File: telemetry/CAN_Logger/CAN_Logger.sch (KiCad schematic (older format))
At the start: 41 parts, among them J1 CONN_02X03, U1 MCP2561-E_SN, U101 TPS560430YF, U2 ATMEGA16M1, Y1 Crystal_SMD

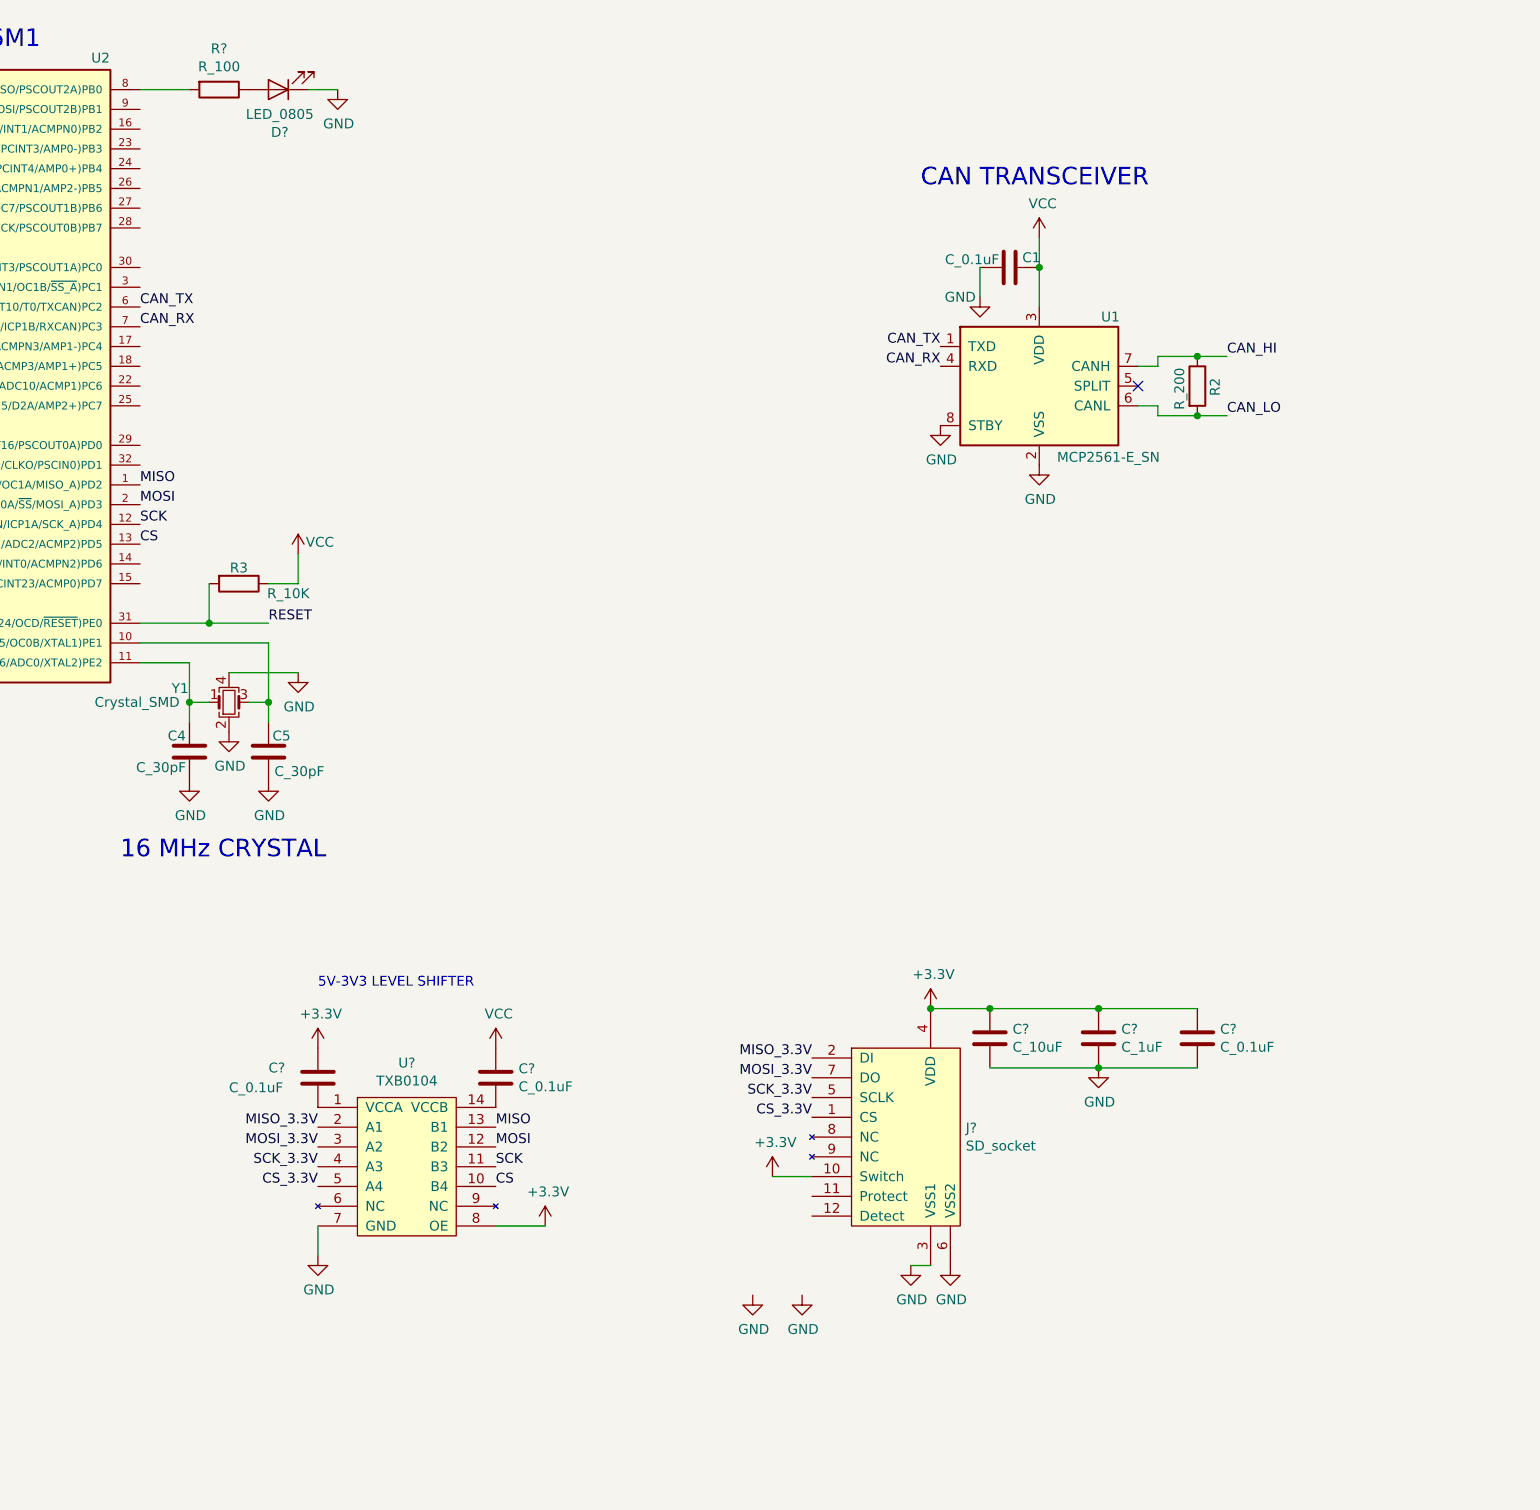
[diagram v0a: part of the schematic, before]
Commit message: ATMEGA LEDs, SD Pro/Detect
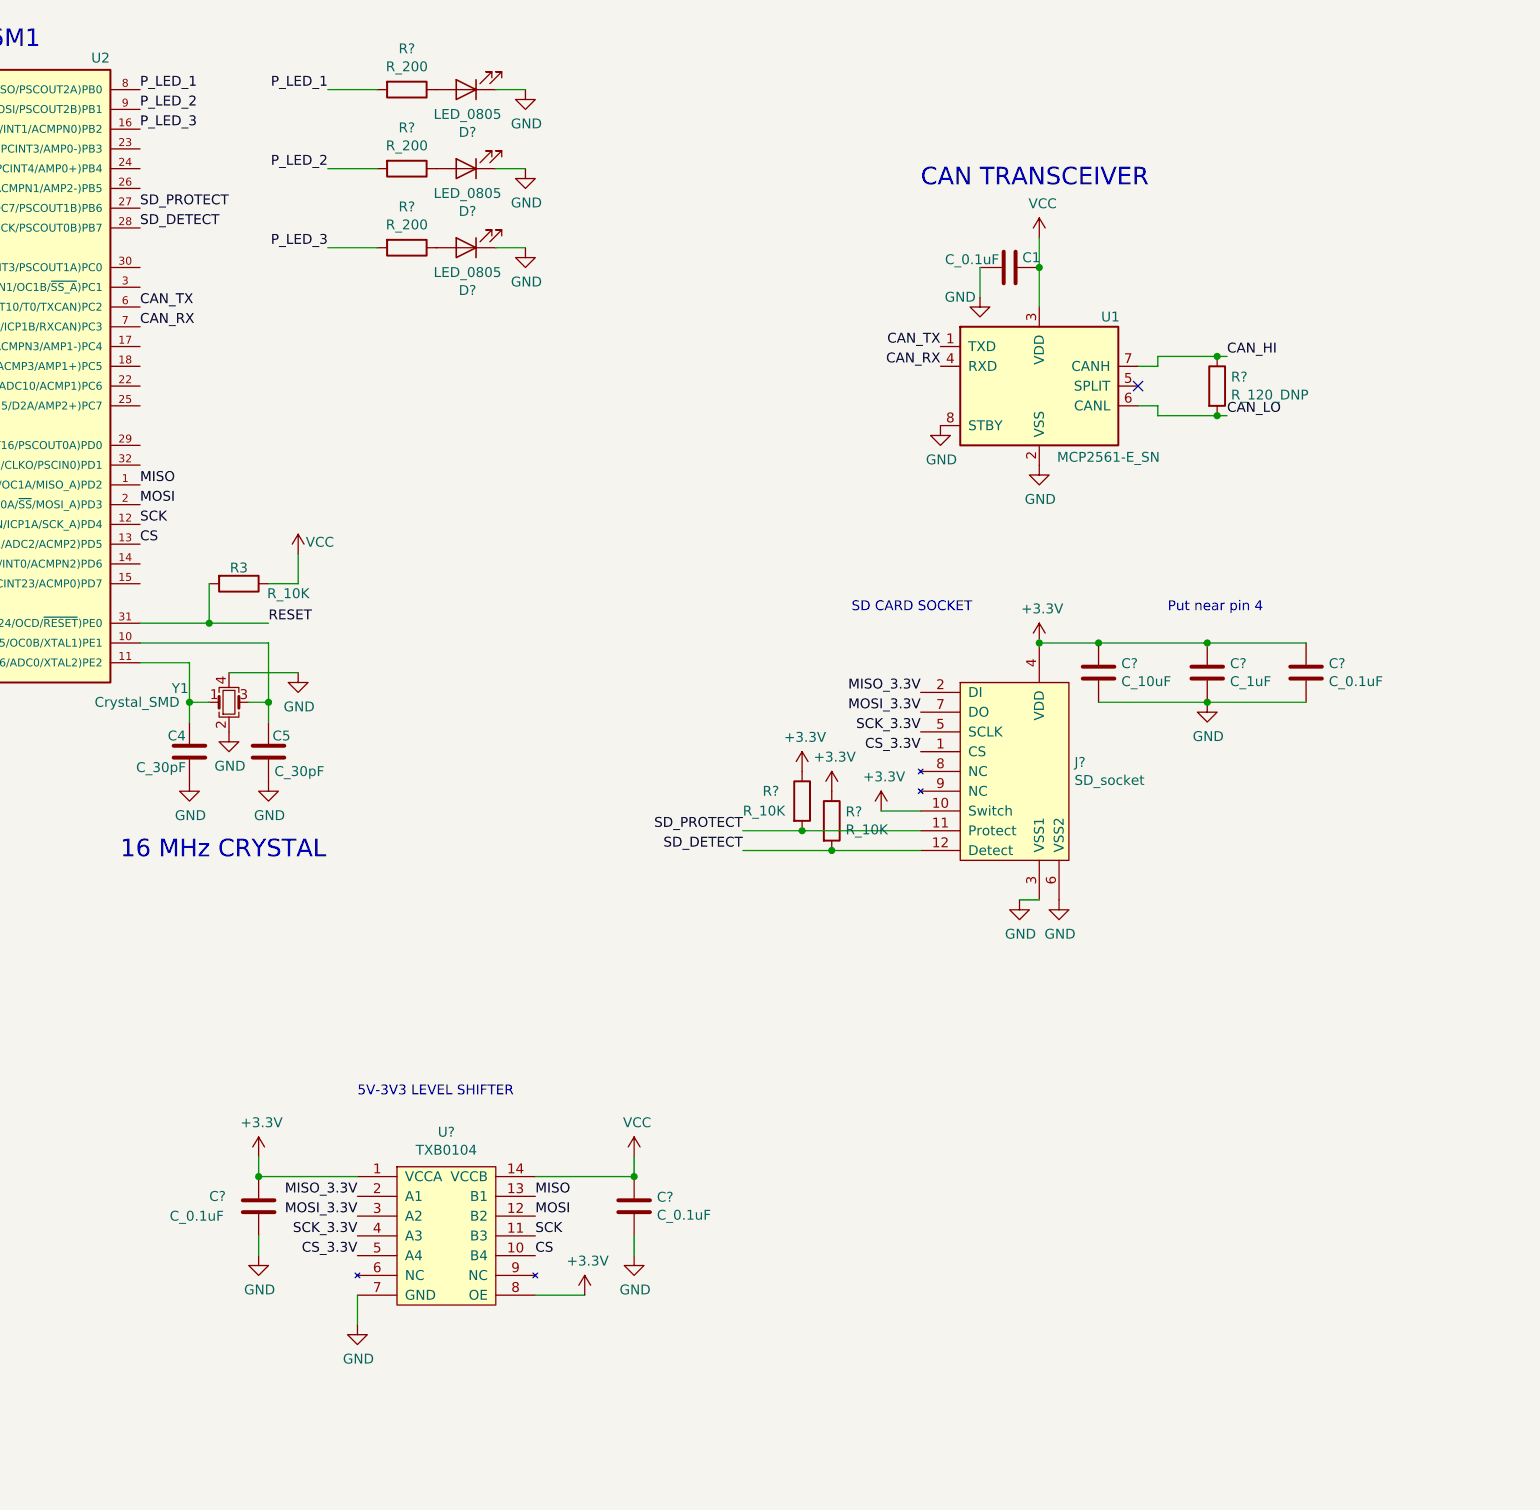
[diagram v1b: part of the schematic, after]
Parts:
- removed R2: R_200, footprints:R_0805_OEM, symbol template-rescue:R_200-formula
- removed R?: R_100, footprints:R_0805_OEM, symbol formula:R_100
- added D? (x2): LED_0805, footprints:LED_0805_OEM, symbol formula:LED_0805
- added R? (x3): R_200, footprints:R_0805_OEM, symbol formula:R_200
- added R?: R_120_DNP, footprints:R_0805_OEM, symbol formula:R_120_DNP
- added R? (x2): R_10K, footprints:R_0805_OEM, symbol formula:R_10K
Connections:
- net +3V3: now also U?.1 (VCCA), R?.1, R?.1
- net CAN_HI: now also R?.1
- net CAN_LO: now also R?.2
- net GND: now also C?.2, C?.2, D?.1 (K), D?.1 (K)
- net VCC: now also U?.14 (VCCB)
- net P_LED_3: now reaches U2.16 ((PCINT2/ADC5/INT1/ACMPN0)PB2)
- net P_LED_3: now also R?.2
- net SD_PROTECT: now reaches U2.27 ((PCINT6/ADC7/PSCOUT1B)PB6)
- net SD_PROTECT: now also J?.11 (Protect), R?.2
- net SD_DETECT: now reaches U2.28 ((PCINT7/ADC4/SCK/PSCOUT0B)PB7)
- net SD_DETECT: now also J?.12 (Detect), R?.2
- net P_LED_1: now reaches U2.8 ((PCINT0/MISO/PSCOUT2A)PB0)
- net P_LED_1: now also R?.2
- net P_LED_2: now reaches U2.9 ((PCINT1/MOSI/PSCOUT2B)PB1)
- net P_LED_2: now also R?.2
- net at D?.2 (A): now also R?.1
- new net: D?.2 (A), R?.1 (x2)
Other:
- note added: "Put near pin 4"
- note added: "SD CARD SOCKET"
- moved on the sheet: C?, D?, J?, U?
